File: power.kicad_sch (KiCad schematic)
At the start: 28 parts, among them U1 MX6UL-VM, U2 MC32PF1510A6EP

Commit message: move to hierarchal labels, work on power tree, add basic pcb layout
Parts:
- removed C? (x2): 0.1uF, Capacitor_SMD:C_0402_1005Metric, symbol Device:C
- removed C? (x7): 10uF, Capacitor_SMD:C_0603_1608Metric, symbol Device:C
- removed C? (x4): 1uF, Capacitor_SMD:C_0402_1005Metric, symbol Device:C
- removed C? (x2): 22uF, Capacitor_SMD:C_0603_1608Metric, symbol Device:C
- removed C?: 0.47uF, Capacitor_SMD:C_0402_1005Metric, symbol Device:C
- removed C? (x2): 4.7uF, Capacitor_SMD:C_0402_1005Metric, symbol Device:C
- removed C?: 2.2uF, Capacitor_SMD:C_0402_1005Metric, symbol Device:C
- removed L? (x3): 1uH, symbol Device:L
- removed R? (x3): 100K, Resistor_SMD:R_0402_1005Metric, symbol Device:R
- removed TP?: TestPoint, symbol Connector:TestPoint
- removed U1: MX6UL-VM, imx6ull-sbc:SOT1534-2, symbol imx6ull-sbc:MX6UL-VM
- removed U2: MC32PF1510A6EP, Package_DFN_QFN:QFN-40-1EP_5x5mm_P0.4mm_EP3.8x3.8mm_ThermalVias, symbol imx6ull-sbc:MC32PF1510A6EP
- added BT1: Battery_Cell, Battery:BatteryHolder_LINX_BAT-HLD-012-SMT, symbol Device:Battery_Cell
- added C1, C11, C12, C13, C14, C16, C17, C18, C9: 1uF, Capacitor_SMD:C_0402_1005Metric, symbol Device:C
- added C15: 0.1uF, Capacitor_SMD:C_0402_1005Metric, symbol Device:C
- added C19, C6, C7, C8: 10uF, Capacitor_SMD:C_0402_1005Metric, symbol Device:C
- added C3: 0.22uF, Capacitor_SMD:C_0402_1005Metric, symbol Device:C
- added C5: 4.7uF, Capacitor_SMD:C_0402_1005Metric, symbol Device:C
- added D6, D7, D8: PMEG3010AESBYL, Diode_SMD:D_SOD-323F, symbol Device:D_Schottky
- added L1: 2.2uH, Inductor_SMD:L_Vishay_IHLP-2020, symbol Device:L
- added R16, R26, R8: 100K, Resistor_SMD:R_0402_1005Metric, symbol Device:R
- added R23: 0R, Resistor_SMD:R_0402_1005Metric, symbol Device:R
- added R24: 499K, Resistor_SMD:R_0402_1005Metric, symbol Device:R
- added R25: 442K, Resistor_SMD:R_0402_1005Metric, symbol Device:R
- added R48, R54: 0R, Resistor_SMD:R_0603_1608Metric, symbol Device:R
- added R56: 1K, Resistor_SMD:R_0402_1005Metric, symbol Device:R
- added R6: 10K, Resistor_SMD:R_0402_1005Metric, symbol Device:R
- added R7: 1M, Resistor_SMD:R_0402_1005Metric, symbol Device:R
- added TP1, TP15, TP16, TP17, TP18, TP19, TP20: TestPoint, TestPoint:TestPoint_Pad_D1.0mm, symbol Connector:TestPoint
- added U19, U2, U20: TLV62569DDC, Package_TO_SOT_SMD:SOT-23-6, symbol Regulator_Switching:TLV62569DDC
- added U21: TPS7A0333DBVR, Package_TO_SOT_SMD:SOT-23-5, symbol Regulator_Linear:TPS7A0533PDBV
- added U22: NCP161BMX330TBG, imx6ull-sbc:XDFN4-1EP_1.0x1.0mm_EP0.52x0.52mm, symbol imx6ull-sbc:NCP161BMX330TBG
- added U23: NCP167AMX180TBG, imx6ull-sbc:XDFN4-1EP_1.0x1.0mm_EP0.52x0.52mm, symbol imx6ull-sbc:NCP167AMX180TBG
- added U24: NCP164CSNADJT1G, Package_SO:TSOP-5_1.65x3.05mm_P0.95mm, symbol imx6ull-sbc:NCP164CSNADJT1G
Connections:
- net DCDC_3V3: now also R48.2, TP17.1
- net GND: now also BT1.2 (-), C11.2, C12.2, C13.2, C14.2, C15.2, C16.2, C17.2, C18.2, C19.2, C3.2, C5.2, C6.2, C7.2, C8.2, C9.2, R16.2, R26.2, R7.2, U19.2 (GND), U21.2 (GND), U22.2 (GND), U22.5 (GND), U23.2 (GND), U23.5 (GND), U24.2 (GND)
- net VSYS_5V: now also C11.1, C12.1, C5.1, C9.1, R24.1, R8.1, U19.4 (VIN), U20.4 (VIN), U21.1 (IN), U21.3 (EN), U22.4 (IN), U23.4 (IN)
- new net: C17.1, R54.1, U23.1 (OUT)
- new net: C6.1, C7.1, C8.1, L1.2, R25.1, R48.1
- new net: C13.1, U24.1 (VIN)
- new net: C18.1, U24.5 (VOUT)
- new net: BT1.1 (+), C15.1, C19.1, D8.2 (A), R56.2
- new net: C1.2, D6.1 (K), R7.1
- new net: L1.1, U19.3 (SW)
- new net: R25.2, R26.1, U19.6 (FB)
- new net: D6.2 (A), R23.1
- new net: C3.1, R16.1, R23.2, R6.2, R8.2, U19.1 (EN)
- new net LDO_1V8: R54.2, TP19.1
- new net LDO_3V3: C16.1, U22.1 (OUT)
- new net PG_3V3: R24.2, TP1.1, U19.5 (PG), U20.1 (EN), U22.3 (EN), U23.3 (EN), U24.3 (EN)
- new net PMIC_ON_REQ: R6.1
- new net SNVS_3V3: D7.1 (K), D8.1 (K), R56.1, TP20.1
- new net VDD_SNVS_3V3: C14.1, D7.2 (A), U21.5 (OUT)
- new net ~{WDOG}: C1.1
- no-connect marks 6 -> 0
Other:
- note added: "Check if Needed"

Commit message: most of sch done, inital component pcb placement
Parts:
- added C114, C115: 4.7uF, Capacitor_SMD:C_0402_1005Metric, symbol Device:C
- added C116, C117, C118, C119, C120, C121: 10uF, Capacitor_SMD:C_0402_1005Metric, symbol Device:C
- added L2, L3: 2.2uH, Inductor_SMD:L_Vishay_IHLP-2020, symbol Device:L
- added Q2, Q3, Q4: 2SK3019, Package_TO_SOT_SMD:SOT-416, symbol imx6ull-sbc:2SK3019
- added R110, R111, R117, R123, R124, R60: 100K, Resistor_SMD:R_0402_1005Metric, symbol Device:R
- added R116: 953K, Resistor_SMD:R_0402_1005Metric, symbol Device:R
- added R118: 91K, Resistor_SMD:R_0402_1005Metric, symbol Device:R
- added R119, R120, R121, R126, R127: 0R, Resistor_SMD:R_0603_1608Metric, symbol Device:R
- added R122: 200K, Resistor_SMD:R_0402_1005Metric, symbol Device:R
- added R125: 93.1K, Resistor_SMD:R_0402_1005Metric, symbol Device:R
- added R59: 124K, Resistor_SMD:R_0402_1005Metric, symbol Device:R
- added R61: 133K, Resistor_SMD:R_0402_1005Metric, symbol Device:R
- added TP27, TP28, TP29: TestPoint, TestPoint:TestPoint_Pad_D1.0mm, symbol Connector:TestPoint
- R16: DNP DNP -> (none)
- R8: DNP (none) -> DNP
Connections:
- net DCDC_3V3: no longer TP17.1
- net DDR_1V35: now also R119.2
- net GND: now also U2.2 (GND), U20.2 (GND), C114.2, C115.2, C116.2, C117.2, C118.2, C119.2, C120.2, C121.2, R110.2, R111.2, R117.2, R123.2, R124.2, R60.2
- net LDO_1V8: no longer TP19.1
- net LDO_3V3: now also R121.2; no longer C16.1, U22.1 (OUT)
- net PG_3V3: now also U2.1 (EN)
- net SD1_VSELECT: now also Q4.2 (G), R124.1
- net SD_3V3_1V8: now also R126.2
- net SNVS_3V3: now also R127.2; no longer D7.1 (K), D8.1 (K), R56.1, TP20.1
- net VDD_ARM_SOC_IN: now also R120.2
- net VSYS_5V: now also U2.4 (VIN), C114.1, C115.1
- net LDO_1V8_R: now reaches C17.1, R54.1, U23.1 (OUT)
- net LDO_1V8_R: now also TP19.1
- net DCDC_3V3_R: now reaches C6.1, C7.1, C8.1, L1.2, R25.1, R48.1
- net DCDC_3V3_R: now also TP17.1
- net at U24.4 (ADJ): now also Q4.1 (S), R122.2, R123.1
- net SD_3V3_1V8_R: now reaches C18.1, U24.5 (VOUT)
- net SD_3V3_1V8_R: now also TP18.1, R122.1, R125.1, R126.1
- net DDR_PG: now reaches TP16.1
- net DDR_PG: now also U20.5 (PG)
- net DDR_1V35_R: now reaches TP15.1
- net DDR_1V35_R: now also C116.1, C117.1, C118.1, L2.2, R119.1, R59.1
- net at U2.3 (SW): now also L3.1
- net ARM_SOC_PG: now reaches U2.5 (PG)
- net ARM_SOC_PG: now also TP27.1
- net at U2.6 (FB): now also Q2.1 (S), Q3.1 (S), R110.1, R61.2
- net at U20.3 (SW): now also L2.1
- net at U20.6 (FB): now also R59.2, R60.1
- new net: Q4.3 (D), R125.2
- new net: D7.1 (K), D8.1 (K), R127.1, R56.1, TP20.1
- new net: Q3.3 (D), R118.2
- new net: Q2.3 (D), R116.2
- new net GPIO_DVFS: Q2.2 (G), R111.1
- new net LDO_3V3_R: C16.1, R121.1, TP29.1, U22.1 (OUT)
- new net PMIC_STBY_REQ: Q3.2 (G), R117.1
- new net VDD_ARM_SOC_IN_R: C119.1, C120.1, C121.1, L3.2, R116.1, R118.1, R120.1, R61.1, TP28.1
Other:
- note added: "PMIC_STBY_REQ = 0, GPIO_DVFS = 0, Vout = 1.4V, R1 = 133k, R2 = 100k PMIC_STBY_REQ = 0, GPIO_DVFS = 1, Vout = 1.3V, R1 = 116.7k, R2 = 100k PMIC_STBY_REQ = 1, GPIO_DVFS = 0, Vout = 0.925V, R1 = 54k, R2 = 100k"
- note added: "SD1_VSELECT = 0, Vout = 3.3V, R1 = 200k, R2 = 100k SD1_VSELECT = 1, Vout = 1.8V, R1 = 63.5k, R2 = 100k"
- moved on the sheet: TP15, TP17, TP18, TP19, TP20, U2

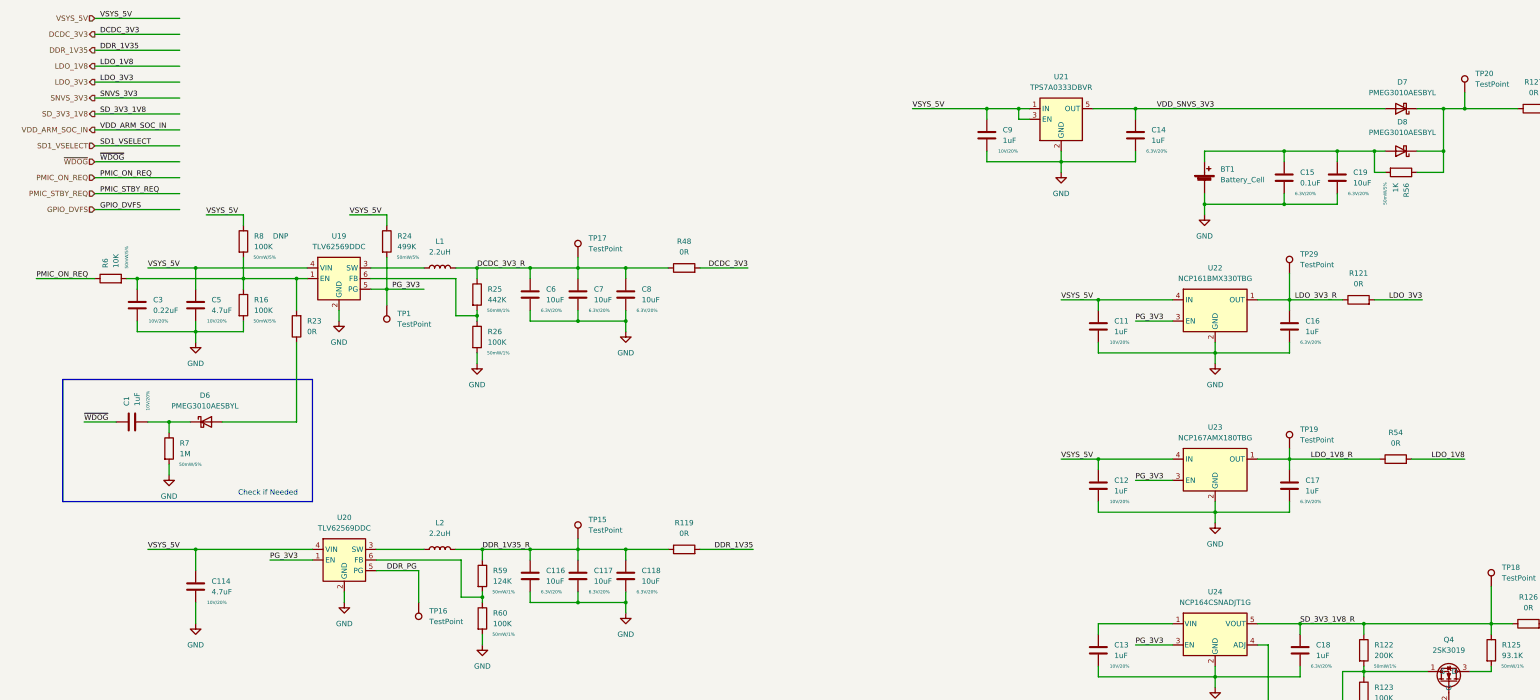
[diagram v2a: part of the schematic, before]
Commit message: lots of routing, ddr length matching done
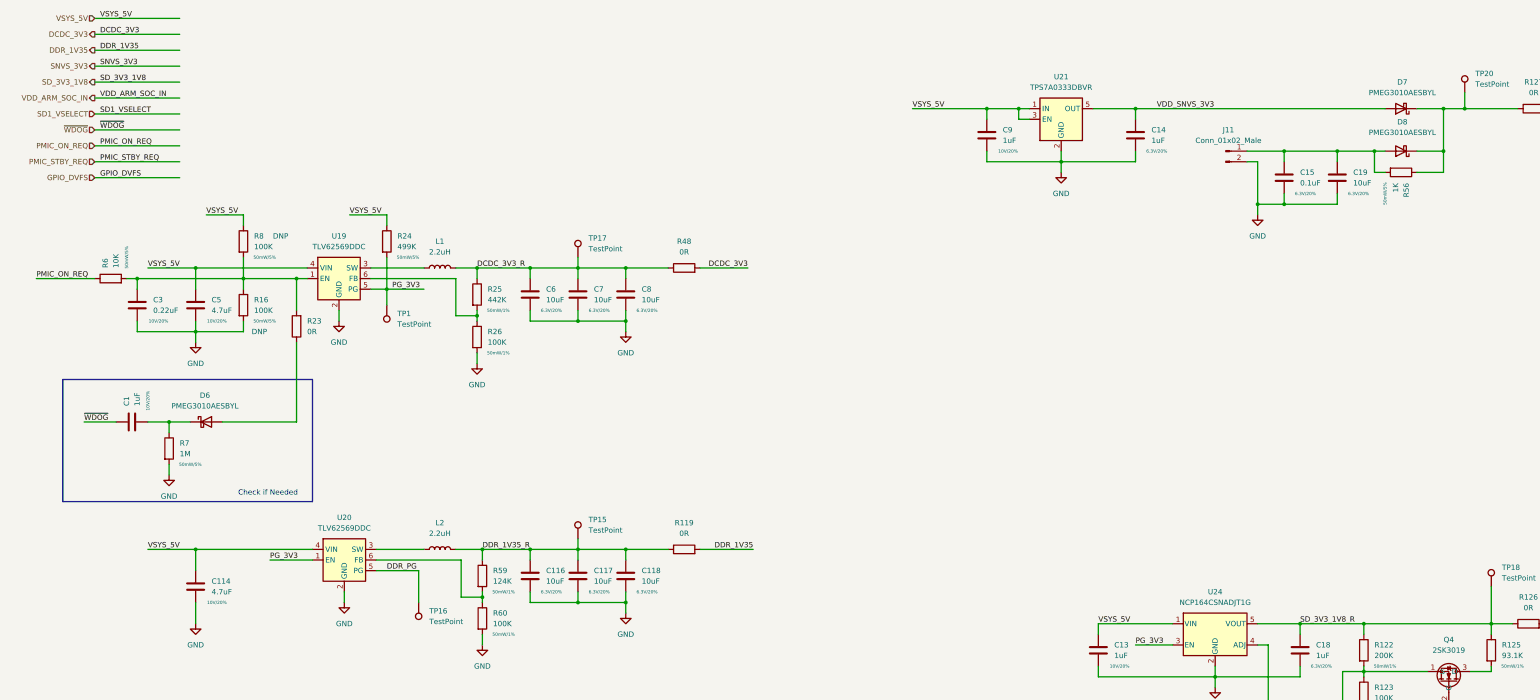
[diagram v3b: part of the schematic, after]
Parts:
- removed BT1: Battery_Cell, Battery:BatteryHolder_LINX_BAT-HLD-012-SMT, symbol Device:Battery_Cell
- removed C11, C12, C16, C17: 1uF, Capacitor_SMD:C_0402_1005Metric, symbol Device:C
- removed R121, R54: 0R, Resistor_SMD:R_0603_1608Metric, symbol Device:R
- removed TP19, TP29: TestPoint, TestPoint:TestPoint_Pad_D1.0mm, symbol Connector:TestPoint
- removed U22: NCP161BMX330TBG, imx6ull-sbc:XDFN4-1EP_1.0x1.0mm_EP0.52x0.52mm, symbol imx6ull-sbc:NCP161BMX330TBG
- removed U23: NCP167AMX180TBG, imx6ull-sbc:XDFN4-1EP_1.0x1.0mm_EP0.52x0.52mm, symbol imx6ull-sbc:NCP167AMX180TBG
- added J11: Conn_01x02_Male, Connector_PinHeader_2.54mm:PinHeader_1x02_P2.54mm_Vertical_SMD_Pin1Left, symbol Connector:Conn_01x02_Male
- L1, L2, L3: footprint Inductor_SMD:L_Vishay_IHLP-2020 -> Inductor_SMD:L_Vishay_IHLP-1212
- Q2, Q3, Q4: symbol imx6ull-sbc:2SK3019 -> qsbc-zero:2SK3019
- R16: DNP (none) -> DNP
- U24: symbol imx6ull-sbc:NCP164CSNADJT1G -> qsbc-zero:NCP164CSNADJT1G
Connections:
- net GND: now also J11.2 (Pin_2)
- net VSYS_5V: now also C13.1, U24.1 (VIN)
- net at C15.1, C19.1, D8.2 (A)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: now also J11.1 (Pin_1)

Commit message: more pcb work, bom work
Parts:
- removed Q2, Q3, Q4: 2SK3019, Package_TO_SOT_SMD:SOT-416, symbol qsbc-zero:2SK3019
- removed U24: NCP164CSNADJT1G, Package_SO:TSOP-5_1.65x3.05mm_P0.95mm, symbol qsbc-zero:NCP164CSNADJT1G
- added Q1, Q2, Q3: SSM3K15ACT, Package_TO_SOT_SMD:SOT-883, symbol qsbc-zero:SSM3K15ACT
- added U10: AP7330, qsbc-zero:SOT-753, symbol qsbc-zero:AP7330
- C1, C13, C9: DigiKey_PN (none) -> 490-13409-1-ND; MPN (none) -> GCM155C71A105KE38D
- C114, C115, C5: DigiKey_PN (none) -> 1276-1482-1-ND; MPN (none) -> CL05A475MP5NRNC
- C116, C117, C118, C119, C120, C121, C19, C6, C7, C8: DigiKey_PN (none) -> 490-GRM155R60J106ME05DCT-ND; MPN (none) -> GRM155R60J106ME05D
- C14, C18: DigiKey_PN (none) -> 490-13409-1-ND; MPN (none) -> GCM155C71A105KE38D; Rating 6.3V/20% -> 10V/20%
- C15: DigiKey_PN (none) -> 490-14603-1-ND; MPN (none) -> GRM155R71E104KE14J; Rating 6.3V/20% -> 25V/20%
- C3: DigiKey_PN (none) -> 490-12706-1-ND; MPN (none) -> GRM155R71A224KE01D
- D6, D7, D8: DigiKey_PN (none) -> 1727-2401-1-ND; MPN (none) -> PMEG3010AESBYL
- J11: footprint Connector_PinHeader_2.54mm:PinHeader_1x02_P2.54mm_Vertical_SMD_Pin1Left -> Connector_PinHeader_2.54mm:PinHeader_1x02_P2.54mm_Vertical; DigiKey_PN (none) -> S1011EC-02-ND; MPN (none) -> PRPC002SAAN-RC
- L1, L2, L3: DigiKey_PN (none) -> 541-1322-1-ND; MPN IHLP2020CZER2R2M11 -> IHLP1212BZER2R2M11
- R110, R123, R26, R60: DigiKey_PN (none) -> CR0402-FX-1003GLFCT-ND; MPN (none) -> CR0402-FX-1003GLF
- R111, R117, R124, R16, R8: DigiKey_PN (none) -> CR0402-FX-1003GLFCT-ND; MPN (none) -> CR0402-FX-1003GLF; Rating 50mW/5% -> 50mW/1%
- R116: DigiKey_PN (none) -> YAG3262CT-ND; MPN (none) -> RC0402FR-07953KL
- R118: DigiKey_PN (none) -> 311-91.0KLRCT-ND; MPN (none) -> RC0402FR-0791KL
- R119, R120, R126, R127, R48: DigiKey_PN (none) -> 311-0.0HRCT-ND; MPN (none) -> RC0603FR-070RL
- R122: value 200K -> 316K; DigiKey_PN (none) -> YAG3113CT-ND; MPN (none) -> RC0402FR-07316KL
- R125: value 93.1K -> 210K; DigiKey_PN (none) -> 311-210KLRCT-ND; MPN (none) -> RC0402FR-07210KL
- R23: DigiKey_PN (none) -> 311-0.0LRCT-ND; MPN (none) -> RC0402FR-070RL
- R24: DigiKey_PN (none) -> 311-499KLRCT-ND; MPN (none) -> RC0402FR-07499KL; Rating 50mW/5% -> 50mW/1%
- R25: DigiKey_PN (none) -> 311-442KLRCT-ND; MPN (none) -> RC0402FR-07442KL
- R56: DigiKey_PN (none) -> 311-1.0KJRCT-ND; MPN (none) -> RC0402JR-071KL
- R59: DigiKey_PN (none) -> 311-124KLRCT-ND; MPN (none) -> RC0402FR-07124KL
- R6: DigiKey_PN (none) -> 311-10KJRCT-ND; MPN (none) -> RC0402JR-0710KL
- R61: DigiKey_PN (none) -> YAG5259CT-ND; MPN (none) -> AC0402FR-07133KL
- R7: DigiKey_PN (none) -> 311-1.0MJRCT-ND; MPN (none) -> RC0402JR-071ML
- U19, U2, U20: DigiKey_PN (none) -> 296-48175-1-ND; MPN (none) -> TLV62569PDDCR
- U21: DigiKey_PN (none) -> 296-TPS7A0333DBVRCT-ND; MPN (none) -> TPS7A0333DBVR
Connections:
- net GND: now also U10.2 (GND)
- net GPIO_DVFS: now also Q1.1 (G)
- net PG_3V3: now also U10.3 (EN)
- net PMIC_STBY_REQ: now also Q2.1 (G)
- net SD1_VSELECT: now also Q3.1 (G)
- net SD_3V3_1V8_R: now also U10.5 (VOUT)
- net VSYS_5V: now also U10.1 (VIN)
- net at R122.2, R123.1: now also Q3.2 (S), U10.4 (ADJ)
- net at R125.2: now also Q3.3 (D)
- net at R110.1, R61.2, U2.6 (FB): now also Q1.2 (S), Q2.2 (S)
- net at R118.2: now also Q2.3 (D)
- net at R116.2: now also Q1.3 (D)

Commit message: add basic readme, rev 1 of pcb
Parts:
- removed C114, C115: 4.7uF, Capacitor_SMD:C_0402_1005Metric, symbol Device:C
- removed C116, C117, C118, C119, C120, C121: 10uF, Capacitor_SMD:C_0402_1005Metric, symbol Device:C
- removed D6, D7, D8: PMEG3010AESBYL, Diode_SMD:D_SOD-323F, symbol Device:D_Schottky
- removed J11: Conn_01x02_Male, Connector_PinHeader_2.54mm:PinHeader_1x02_P2.54mm_Vertical, symbol Connector:Conn_01x02_Male
- removed Q1, Q2, Q3: SSM3K15ACT, Package_TO_SOT_SMD:SOT-883, symbol qsbc-zero:SSM3K15ACT
- removed R110, R111, R117, R123, R124, R26, R60: 100K, Resistor_SMD:R_0402_1005Metric, symbol Device:R
- removed R116: 953K, Resistor_SMD:R_0402_1005Metric, symbol Device:R
- removed R118: 91K, Resistor_SMD:R_0402_1005Metric, symbol Device:R
- removed R119, R120, R126, R127, R48: 0R, Resistor_SMD:R_0603_1608Metric, symbol Device:R
- removed R122: 316K, Resistor_SMD:R_0402_1005Metric, symbol Device:R
- removed R125: 210K, Resistor_SMD:R_0402_1005Metric, symbol Device:R
- removed R56: 1K, Resistor_SMD:R_0402_1005Metric, symbol Device:R
- removed R59: 124K, Resistor_SMD:R_0402_1005Metric, symbol Device:R
- removed R61: 133K, Resistor_SMD:R_0402_1005Metric, symbol Device:R
- removed TP1, TP15, TP16, TP17, TP18, TP20, TP27, TP28: TestPoint, TestPoint:TestPoint_Pad_D1.0mm, symbol Connector:TestPoint
- removed U10: AP7330, qsbc-zero:SOT-753, symbol qsbc-zero:AP7330
- removed U19, U2, U20: TLV62569DDC, Package_TO_SOT_SMD:SOT-23-6, symbol Regulator_Switching:TLV62569DDC
- removed U21: TPS7A0333DBVR, Package_TO_SOT_SMD:SOT-23-5, symbol Regulator_Linear:TPS7A0533PDBV
- added C11, C12: 22uF, Capacitor_SMD:C_0603_1608Metric, symbol Device:C
- added C16, C20, C84: 10uF, Capacitor_SMD:C_0402_1005Metric, symbol Device:C
- added C17, C21, C87, C89, C91: 4.7uF, Capacitor_SMD:C_0402_1005Metric, symbol Device:C
- added C22, C88, C90, C96: 1uF, Capacitor_SMD:C_0402_1005Metric, symbol Device:C
- added C83: 0.47uF, Capacitor_SMD:C_0402_1005Metric, symbol Device:C
- added J8: Conn_01x09_Male, Connector_PinHeader_1.27mm:PinHeader_1x09_P1.27mm_Vertical, symbol Connector:Conn_01x09_Male
- added J9: Conn_01x02_Male, Connector_PinHeader_2.54mm:PinHeader_1x02_P2.54mm_Vertical, symbol Connector:Conn_01x02_Male
- added SW1: SW_Push, Button_Switch_THT:SW_Tactile_SPST_Angled_PTS645Vx58-2LFS, symbol Switch:SW_Push
- added TP4: TestPoint, TestPoint:TestPoint_Pad_D1.0mm, symbol Connector:TestPoint
- added U2: MC32PF1510A6EP, Package_DFN_QFN:QFN-40-1EP_5x5mm_P0.4mm_EP3.8x3.8mm_ThermalVias, symbol qsbc-zero:MC32PF1510A6EP
- C1: value 1uF -> 0.1uF; DigiKey_PN 490-13409-1-ND -> 490-14603-1-ND; MPN GCM155C71A105KE38D -> GRM155R71E104KE14J; Rating 10V/20% -> 25V/20%
- C13, C14, C18: value 1uF -> 10uF; DigiKey_PN 490-13409-1-ND -> 490-GRM155R60J106ME05DCT-ND; MPN GCM155C71A105KE38D -> GRM155R60J106ME05D; Rating 10V/20% -> 6.3V/20%
- C15: value 0.1uF -> 10uF; DigiKey_PN 490-14603-1-ND -> 490-GRM155R60J106ME05DCT-ND; MPN GRM155R71E104KE14J -> GRM155R60J106ME05D; Rating 25V/20% -> 6.3V/20%
- C3: value 0.22uF -> 10uF; DigiKey_PN 490-12706-1-ND -> 490-GRM155R60J106ME05DCT-ND; MPN GRM155R71A224KE01D -> GRM155R60J106ME05D; Rating 10V/20% -> 6.3V/20%
- C5: value 4.7uF -> 0.1uF; DigiKey_PN 1276-1482-1-ND -> 490-14603-1-ND; MPN CL05A475MP5NRNC -> GRM155R71E104KE14J; Rating 10V/20% -> 25V/20%
- C6, C8: value 10uF -> 1uF; DigiKey_PN 490-GRM155R60J106ME05DCT-ND -> 490-13409-1-ND; MPN GRM155R60J106ME05D -> GCM155C71A105KE38D
- C7: value 10uF -> 2.2uF; DigiKey_PN 490-GRM155R60J106ME05DCT-ND -> 1276-1469-1-ND; MPN GRM155R60J106ME05D -> CL05A225MQ5NNNC; Rating 6.3V/20% -> 10V/20%
- C9: Rating 10V/20% -> 6.3V/20%
- L1, L2, L3: value 2.2uH -> 1uH; footprint Inductor_SMD:L_Vishay_IHLP-1212 -> Inductor_SMD:L_0603_1608Metric; DigiKey_PN 541-1322-1-ND -> 490-DFE18SBN1R0ME0LCT-ND; MPN IHLP1212BZER2R2M11 -> DFE18SBN1R0ME0L
- R16, R8: DNP DNP -> (none)
- R23: value 0R -> 100K; DigiKey_PN 311-0.0LRCT-ND -> CR0402-FX-1003GLFCT-ND; MPN RC0402FR-070RL -> CR0402-FX-1003GLF; Rating (none) -> 50mW/1%
- R24: value 499K -> 100K; DigiKey_PN 311-499KLRCT-ND -> CR0402-FX-1003GLFCT-ND; MPN RC0402FR-07499KL -> CR0402-FX-1003GLF
- R25: value 442K -> 0R; DigiKey_PN 311-442KLRCT-ND -> 311-0.0LRCT-ND; MPN RC0402FR-07442KL -> RC0402FR-070RL; Rating 50mW/1% -> (none)
- R6: value 10K -> 100K; DigiKey_PN 311-10KJRCT-ND -> CR0402-FX-1003GLFCT-ND; MPN RC0402JR-0710KL -> CR0402-FX-1003GLF; Rating 50mW/5% -> 50mW/1%
- R7: value 1M -> 100K; DigiKey_PN 311-1.0MJRCT-ND -> CR0402-FX-1003GLFCT-ND; MPN RC0402JR-071ML -> CR0402-FX-1003GLF; Rating 50mW/5% -> 50mW/1%
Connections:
- net DDR_1V35_R is gone; now on net DDR_1V35: L2.2
- net SD_3V3_1V8_R is gone; now on net DCDC_3V3: C18.1
- net VDD_ARM_SOC_IN_R is gone; now on net DCDC_3V3: L3.2
- net VDD_SNVS_3V3 is gone; now on net VDD_ARM_SOC_IN: C14.1
- net DCDC_3V3: now also C5.1, R6.1, C20.1, J8.1 (Pin_1), U2.15 (SW3FB), U2.4 (VDDIO)
- net DDR_1V35: now also C15.1, C6.1, C16.1, U2.16 (SW2FB), U2.22 (VINREFDDR)
- net GND: now also C1.2, C11.2, C12.2, C16.2, C17.2, C20.2, C21.2, C22.2, C83.2, C84.2, C87.2, C88.2, C89.2, C90.2, C91.2, C96.2, J8.9 (Pin_9), J9.2 (Pin_2), SW1.1, U2.32 (GND), U2.40 (GND), U2.41 (EP), U2.5 (VDDOTP); no longer R16.2, R7.2
- net PMIC_ON_REQ: now also R25.2, J8.3 (Pin_3); no longer R6.1
- net PMIC_STBY_REQ: now also R8.2, J8.8 (Pin_8), U2.7 (STANDBY)
- net SD_3V3_1V8: now also C21.1, U2.12 (VLDO3)
- net VDD_ARM_SOC_IN: now also C13.1, L1.2, U2.27 (SW1FB)
- net VSYS_5V: now also C7.1, U2.37 (VIN); no longer C13.1, C5.1, C9.1, R24.1, R8.1
- net ~{WDOG}: now also R6.2, U2.1 (WDI); no longer C1.1
- net LDO2_3V3: now reaches C19.1
- net LDO2_3V3: now also U2.19 (VLDO2); no longer C15.1
- net SNVS_3V: now reaches R7.1
- net SNVS_3V: now also R16.1, R23.1, R8.1, C83.1, J8.5 (Pin_5), U2.30 (VSNVS); no longer C1.2
- net at L2.1: now also U2.18 (SW2LX)
- net at L1.1: now also U2.25 (SW1LX)
- net at L3.1: now also U2.13 (SW3LX)
- removed net DCDC_3V3_R: C6.1, C7.1, C8.1, L1.2, R25.1
- net PG_3V3 renamed PMIC_ONOFF
- net PMIC_ONOFF: now also J8.6 (Pin_6), SW1.2, U2.8 (ONKEY)
- new net DDR_VREF: C22.1, U2.21 (VREFDDR)
- new net I2C_SCL: U2.3 (SCL)
- new net I2C_SDA: U2.2 (SDA)
- new net IMX6_ONOFF: J8.7 (Pin_7)
- new net LDO1_1V8: C17.1, TP4.1, U2.29 (VLDO1)
- new net LICELL: C1.1, C3.1, C84.1, J9.1 (Pin_1), U2.31 (LICELL)
- new net PWRON: J8.2 (Pin_2), R25.1, R7.2, U2.6 (PWRON)
- new net VCORE: C8.1, U2.24 (VCORE)
- new net VDIG: C9.1, U2.23 (VDIG)
- new net VSYS: C11.1, C12.1, C87.1, C88.1, C89.1, C90.1, C91.1, C96.1, R24.1, U2.11 (VLDO3IN), U2.14 (SW3IN), U2.17 (SW2IN), U2.20 (VLDO2IN), U2.26 (SW1IN), U2.28 (VLDO1IN), U2.35 (VSYS1), U2.36 (VSYS2)
- new net ~{PMIC_INT}: R16.2, U2.9 (~{INT})
- new net ~{POR}: J8.4 (Pin_4), R23.2, U2.10 (~{RESETBMCU})
- no-connect marks 0 -> 4
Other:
- note removed: "Check if Needed"
- note removed: "PMIC_STBY_REQ = 0, GPIO_DVFS = 0, Vout = 1.4V, R1 = 133k, R2 = 100k PMIC_STBY_REQ = 0, GPIO_DVFS = 1, Vout = 1.3V, R1 = 116.7k, R2 = 100k PMIC_STBY_REQ = 1, GPIO_DVFS = 0, Vout = 0.925V, R1 = 54k, R2 = 100k"
- note removed: "SD1_VSELECT = 0, Vout = 3.3V, R1 = 200k, R2 = 100k SD1_VSELECT = 1, Vout = 1.8V, R1 = 63.5k, R2 = 100k"
